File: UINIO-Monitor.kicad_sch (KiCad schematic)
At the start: 0 parts

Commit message: Start schematic drawing.
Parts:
- added C? (x5): 1uF, Capacitor_SMD:C_0402_1005Metric, symbol Device:C
- added CON? (x2): FFC_8Pin_0.5mm, Uinio:FPC-SMD_8P-P0.5_C9900011879, symbol Uinio:FFC_8Pin_0.5mm
- added D? (x5): 1N5819, Diode_THT:D_DO-41_SOD81_P10.16mm_Horizontal, symbol Diode:1N5819
- added J? (x2): Conn_01x08_Male, symbol Connector:Conn_01x08_Male
- added P?: LCD_Pad_12Pin, Uinio:ST7789-FPC-PAD, symbol Uinio:LCD_Pad_12Pin
- added P?: LCD_Pad_10Pin, symbol Uinio:LCD_Pad_10Pin
- added R?: 10K, symbol Device:R
- added R?: 10R, symbol Device:R
- added R? (x5): 4.7K, symbol Device:R
- added R?: 5.1R, symbol Device:R
- added R?: 20R, symbol Device:R
- added R?: 1K, symbol Device:R
- added U? (x2): ME6211C33M5G-N, Uinio:SOT-23-5_L3.0-W1.7-P0.95-LS2.8-BR, symbol Uinio:ME6211
- added VT?: S8050, Uinio:SOT-23-3_L2.9-W1.6-P1.90-LS2.9-BL, symbol Uinio:S8050
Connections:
- new net: P?.2 (LEDK), R?.2
- new net: C?.2, P?.3 (LEDA), P?.4 (VDD)
- new net: R?.1, R?.2, VT?.1 (B)
- new net: R?.1, VT?.3 (C)
- new net: CON?.1, J?.1 (Pin_1), R?.1
- new net: CON?.2, J?.2 (Pin_2), R?.1
- new net: CON?.3, J?.3 (Pin_3), R?.1
- new net: CON?.4, J?.4 (Pin_4), R?.1
- new net: CON?.5, J?.5 (Pin_5), R?.1
- new net: D?.2 (A), R?.2 (x5)
- new net: P?.1 (GND), R?.2
- new net: P?.9 (LEDA), R?.2
- new net 3.3V_1.3inch: C?.2, CON?.6, J?.6 (Pin_6), R?.1, U?.5 (Vout)
- new net 3.3V_2.4inch: C?.2, CON?.6, D?.1 (K), D?.1 (K), D?.1 (K), D?.1 (K), D?.1 (K), J?.6 (Pin_6), P?.2 (RESET), P?.3 (SCL), P?.4 (D/C), P?.5 (CS), P?.6 (SDA), P?.8 (VCC), U?.5 (Vout)
- new net 5V_1.3inch: C?.2, CON?.8, J?.8 (Pin_8), U?.1 (Vin), U?.3 (CE)
- new net 5V_2.4inch: C?.2, CON?.8, J?.8 (Pin_8), R?.1, U?.1 (Vin), U?.3 (CE)
- new net BLK: R?.2
- new net CS_1.3inch: CON?.1, J?.1 (Pin_1), P?.8 (CS)
- new net D/C_1.3inch: CON?.2, J?.2 (Pin_2), P?.7 (D/C)
- new net GND: C?.1, C?.1, C?.1, C?.1, C?.1, CON?.7, CON?.7, J?.7 (Pin_7), J?.7 (Pin_7), P?.1 (GND), P?.10 (LEDK), P?.12 (GND), P?.5 (GND), P?.6 (GND), R?.1, U?.2 (Vss), U?.2 (Vss), VT?.2 (E)
- new net RESET_1.3inch: CON?.3, J?.3 (Pin_3), P?.11 (RESET)
- new net SCL_1.3inch: CON?.5, J?.5 (Pin_5), P?.9 (SCL)
- new net SDA_1.3inch: CON?.4, J?.4 (Pin_4), P?.10 (SDA)
- no-connect marks 0 -> 3
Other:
- note added: "2.4 英寸"

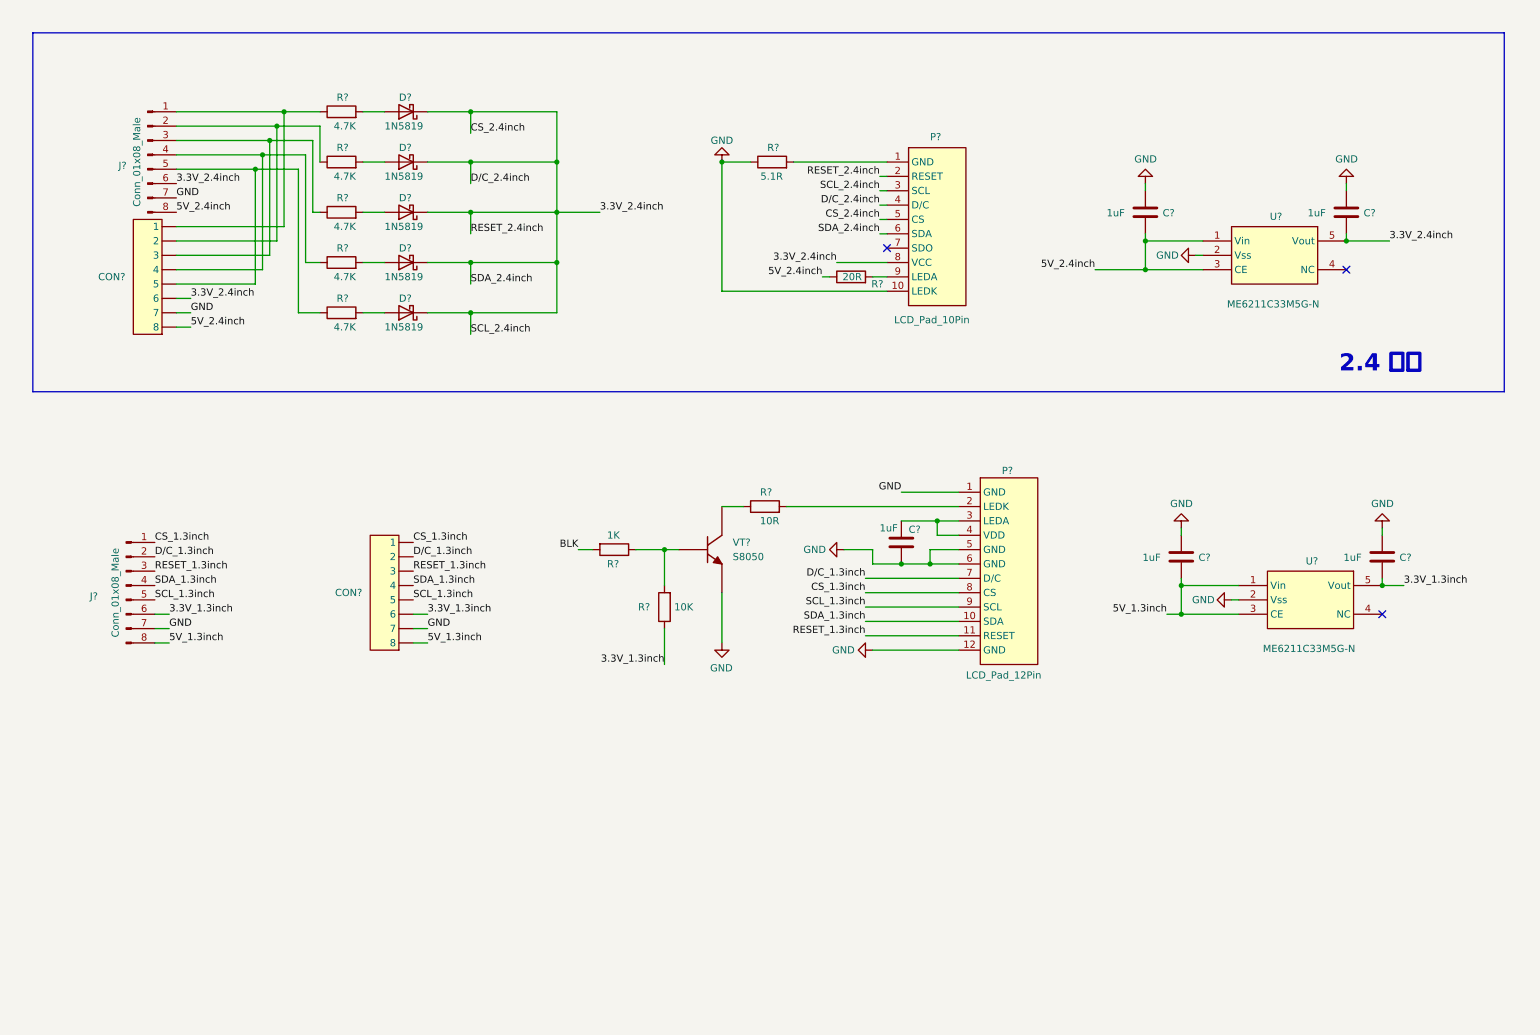
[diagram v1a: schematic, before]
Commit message: Redraw the schematic.
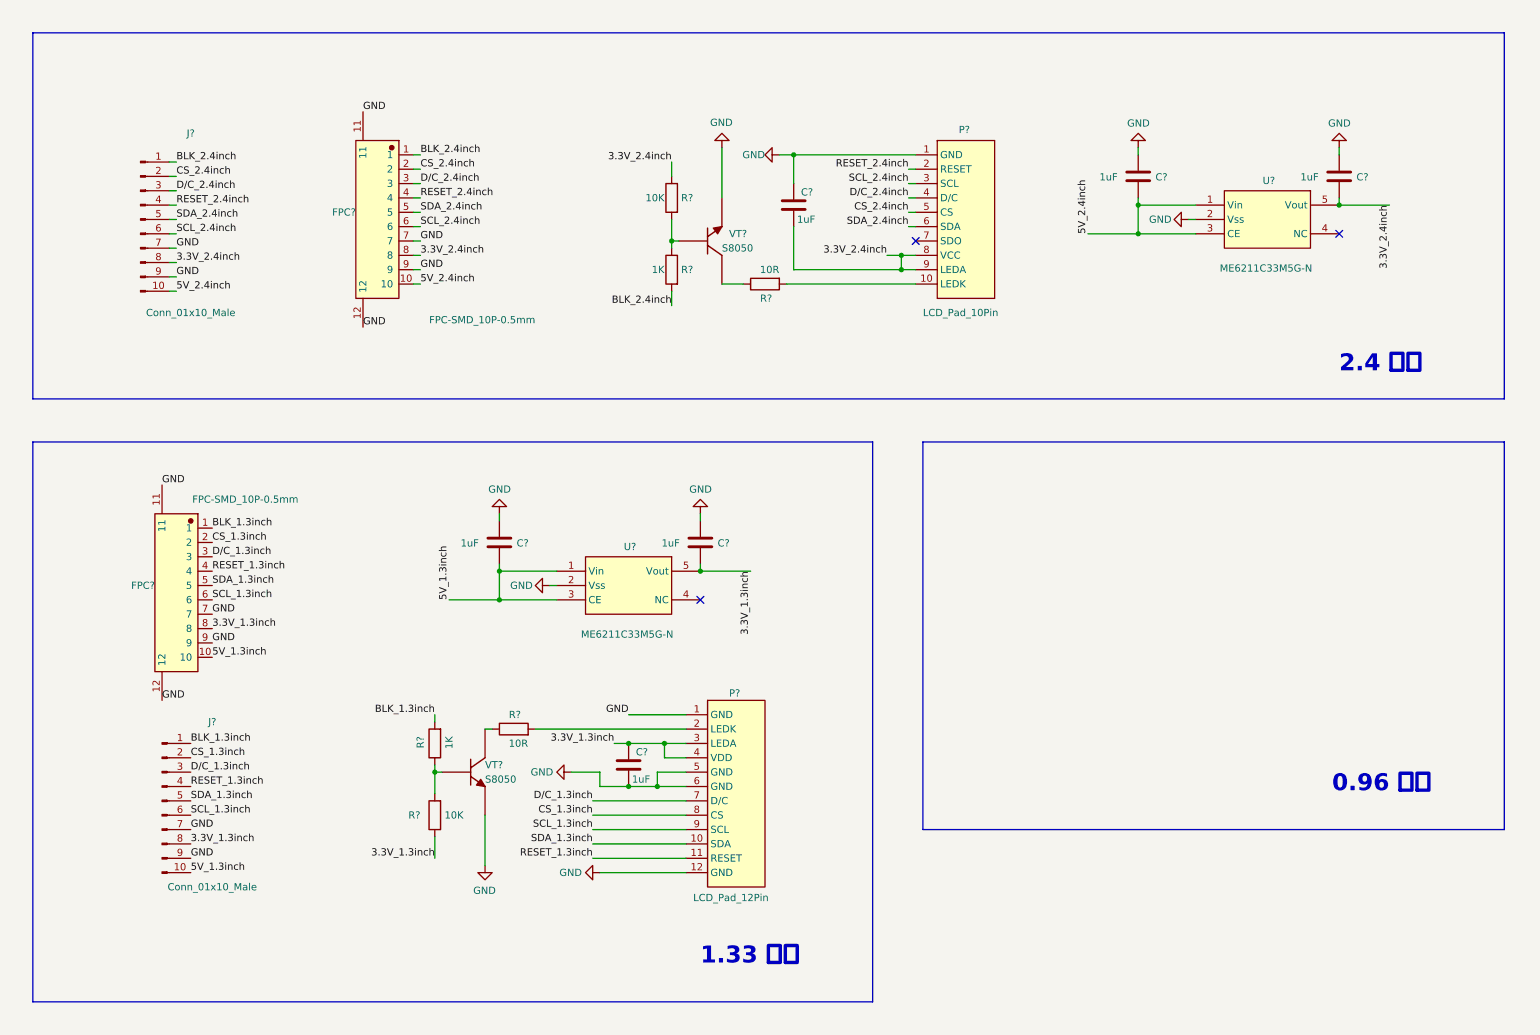
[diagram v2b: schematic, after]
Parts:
- removed C? (x2): 1uF, Capacitor_SMD:C_0402_1005Metric, symbol Device:C
- removed CON? (x2): FFC_8Pin_0.5mm, Uinio:FPC-SMD_8P-P0.5_C9900011879, symbol Uinio:FFC_8Pin_0.5mm
- removed D? (x5): 1N5819, Diode_THT:D_DO-41_SOD81_P10.16mm_Horizontal, symbol Diode:1N5819
- removed J? (x2): Conn_01x08_Male, symbol Connector:Conn_01x08_Male
- removed R? (x5): 4.7K, symbol Device:R
- removed R?: 5.1R, symbol Device:R
- removed R?: 20R, symbol Device:R
- removed U?: ME6211C33M5G-N, Uinio:SOT-23-5_L3.0-W1.7-P0.95-LS2.8-BR, symbol Uinio:ME6211
- added C? (x3): 1uF, Capacitor_SMD:C_0402_1005Metric, symbol Device:C
- added FPC? (x2): FPC-SMD_10P-0.5mm, Uinio:FPC-SMD_KH-FG0.5-H2.0-10Pin, symbol Uinio:FPC-SMD_10P-0.5mm
- added J? (x2): Conn_01x10_Male, symbol Connector:Conn_01x10_Male
- added R?: 10R, symbol Device:R
- added R?: 10K, symbol Device:R
- added R?: 1K, symbol Device:R
- added U?: ME6211C33M5G-N, Uinio:SOT-23-5_L3.0-W1.7-P0.95-LS2.8-BR, symbol Uinio:ME6211
- added VT?: S8050, Uinio:SOT-23-3_L2.9-W1.6-P1.90-LS2.9-BL, symbol Uinio:S8050
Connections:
- net 3.3V_1.3inch: now also C?.2, P?.3 (LEDA), P?.4 (VDD), FPC?.8, J?.8 (Pin_8)
- net 3.3V_2.4inch: now also P?.9 (LEDA), C?.1, C?.2, FPC?.8, J?.8 (Pin_8), R?.1, U?.5 (Vout); no longer P?.2 (RESET), P?.3 (SCL), P?.4 (D/C), P?.5 (CS), P?.6 (SDA)
- net 5V_1.3inch: now also FPC?.10, J?.10 (Pin_10)
- net 5V_2.4inch: now also C?.2, FPC?.10, J?.10 (Pin_10), U?.1 (Vin), U?.3 (CE)
- net CS_1.3inch: now also FPC?.2, J?.2 (Pin_2)
- net D/C_1.3inch: now also FPC?.3, J?.3 (Pin_3)
- net GND: now also P?.1 (GND), C?.1, C?.1, C?.2, FPC?.11, FPC?.11, FPC?.12, FPC?.12, FPC?.7, FPC?.7, FPC?.9, FPC?.9, J?.7 (Pin_7), J?.7 (Pin_7), J?.9 (Pin_9), J?.9 (Pin_9), U?.2 (Vss), VT?.2 (E); no longer P?.10 (LEDK)
- net RESET_1.3inch: now also FPC?.4, J?.4 (Pin_4)
- net SCL_1.3inch: now also FPC?.6, J?.6 (Pin_6)
- net SDA_1.3inch: now also FPC?.5, J?.5 (Pin_5)
- net BLK renamed BLK_1.3inch
- net BLK_1.3inch: now also FPC?.1, J?.1 (Pin_1)
- new net: R?.1, VT?.3 (C)
- new net: P?.10 (LEDK), R?.2
- new net: R?.1, R?.2, VT?.1 (B)
- new net BLK_2.4inch: FPC?.1, J?.1 (Pin_1), R?.2
- new net CS_2.4inch: FPC?.2, J?.2 (Pin_2), P?.5 (CS)
- new net D/C_2.4inch: FPC?.3, J?.3 (Pin_3), P?.4 (D/C)
- new net RESET_2.4inch: FPC?.4, J?.4 (Pin_4), P?.2 (RESET)
- new net SCL_2.4inch: FPC?.6, J?.6 (Pin_6), P?.3 (SCL)
- new net SDA_2.4inch: FPC?.5, J?.5 (Pin_5), P?.6 (SDA)
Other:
- note added: "0.96 英寸"
- note added: "1.33 英寸"
- moved on the sheet: C?, P?, R?, U?, VT?

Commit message: Redraw the schematic.
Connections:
- net 3.3V_1.3inch: now also FPC?.1, J?.1 (Pin_1); no longer FPC?.8, J?.8 (Pin_8)
- net 3.3V_2.4inch: now also FPC?.1, J?.1 (Pin_1); no longer FPC?.8, J?.8 (Pin_8)
- net BLK_1.3inch: now also FPC?.3, J?.3 (Pin_3); no longer FPC?.1, J?.1 (Pin_1)
- net BLK_2.4inch: now also FPC?.3, J?.3 (Pin_3); no longer FPC?.1, J?.1 (Pin_1)
- net CS_1.3inch: now also FPC?.4, J?.4 (Pin_4); no longer FPC?.2, J?.2 (Pin_2)
- net CS_2.4inch: now also FPC?.4, J?.4 (Pin_4); no longer FPC?.2, J?.2 (Pin_2)
- net D/C_1.3inch: now also FPC?.5, J?.5 (Pin_5); no longer FPC?.3, J?.3 (Pin_3)
- net D/C_2.4inch: now also FPC?.5, J?.5 (Pin_5); no longer FPC?.3, J?.3 (Pin_3)
- net GND: now also FPC?.2, FPC?.2, J?.2 (Pin_2), J?.2 (Pin_2); no longer FPC?.7, FPC?.7, J?.7 (Pin_7), J?.7 (Pin_7)
- net RESET_1.3inch: now also FPC?.6, J?.6 (Pin_6); no longer FPC?.4, J?.4 (Pin_4)
- net RESET_2.4inch: now also FPC?.6, J?.6 (Pin_6); no longer FPC?.4, J?.4 (Pin_4)
- net SCL_1.3inch: now also FPC?.8, J?.8 (Pin_8); no longer FPC?.6, J?.6 (Pin_6)
- net SCL_2.4inch: now also FPC?.8, J?.8 (Pin_8); no longer FPC?.6, J?.6 (Pin_6)
- net SDA_1.3inch: now also FPC?.7, J?.7 (Pin_7); no longer FPC?.5, J?.5 (Pin_5)
- net SDA_2.4inch: now also FPC?.7, J?.7 (Pin_7); no longer FPC?.5, J?.5 (Pin_5)
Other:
- moved on the sheet: C?, FPC?, J?, P?, R?, U?, VT?

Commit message: Complete schematic drawing.
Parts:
- removed J? (x2): Conn_01x10_Male, symbol Connector:Conn_01x10_Male
- added C10, C11, C12, C13, C8, C9: C, Capacitor_SMD:C_0402_1005Metric, symbol Device:C
- added C7: C, Capacitor_SMD:C_0603_1608Metric, symbol Device:C
- added D1: 1N4148W, Diode_SMD:D_SOD-123, symbol Diode:1N4148W
- added J1, J2: Conn_01x09_Male, Connector_PinHeader_2.54mm:PinHeader_1x09_P2.54mm_Vertical, symbol Connector:Conn_01x09_Male
- added J3: Conn_01x04_Male, Connector_PinHeader_2.54mm:PinHeader_1x04_P2.54mm_Vertical, symbol Connector:Conn_01x04_Male
- added P3: OLED_Pad_30Pin, Uinio:OLED_Pad_30Pin, symbol Uinio:OLED_Pad_30Pin
- added R10, R7, R8, R9: R, Resistor_SMD:R_0402_1005Metric, symbol Device:R
- added U3: XC6206PxxxMR, Package_TO_SOT_SMD:SOT-23-3, symbol Regulator_Linear:XC6206PxxxMR
- C1, C2, C3, C4, C5, C6: renamed from C?; value 1uF -> C; footprint Capacitor_SMD:C_0402_1005Metric -> Capacitor_SMD:C_0603_1608Metric
- P1: renamed from P?; footprint (none) -> Uinio:LCD_Pad_10Pin
- P2: renamed from P?; footprint Uinio:ST7789-FPC-PAD -> Uinio:LCD_Pad_12Pin
- R1, R4: renamed from R?; value 10K -> R; footprint (none) -> Resistor_SMD:R_0603_1608Metric
- R2, R3: renamed from R?; value 1K -> R; footprint (none) -> Resistor_SMD:R_0603_1608Metric
- R5, R6: renamed from R?; value 10R -> R; footprint (none) -> Resistor_SMD:R_0603_1608Metric
- U1, U2: renamed from U?; value ME6211C33M5G-N -> ME6211
- gave numbers to parts that had none: 4
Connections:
- net 3.3V_1.3inch: now also J1.7 (Pin_7)
- net 3.3V_2.4inch: now also J2.7 (Pin_7)
- net 5V_1.3inch: now also J1.9 (Pin_9)
- net 5V_2.4inch: now also J2.9 (Pin_9)
- net BLK_1.3inch: now also J1.1 (Pin_1)
- net BLK_2.4inch: now also J2.1 (Pin_1)
- net CS_1.3inch: now also J1.2 (Pin_2)
- net CS_2.4inch: now also J2.2 (Pin_2)
- net D/C_1.3inch: now also J1.3 (Pin_3)
- net D/C_2.4inch: now also J2.3 (Pin_3)
- net GND: now also C10.2, C11.2, C7.1, C8.1, C9.1, J1.8 (Pin_8), J2.8 (Pin_8), J3.3 (Pin_3), P3.1 (NC), P3.10 (BS0), P3.12 (BS2), P3.13 (CS), P3.15 (D/C), P3.16 (RW), P3.17 (RD), P3.21 (D3), P3.22 (D4), P3.23 (D5), P3.24 (D6), P3.25 (D7), P3.29 (VLSS), P3.30 (NC), P3.8 (VSS), R10.1, U3.1 (GND)
- net RESET_1.3inch: now also J1.4 (Pin_4)
- net RESET_2.4inch: now also J2.4 (Pin_4)
- net SCL_1.3inch: now also J1.6 (Pin_6)
- net SCL_2.4inch: now also J2.6 (Pin_6)
- net SDA_1.3inch: now also J1.5 (Pin_5)
- net SDA_2.4inch: now also J2.5 (Pin_5)
- new net: C8.2, C9.2, D1.1 (K), P3.11 (BS1), P3.6 (VBAT), P3.9 (VDD), R7.2, R8.2, R9.2, U3.2 (VO)
- new net: C13.1, P3.5 (C1N)
- new net: C13.2, P3.4 (C1P)
- new net: C12.1, P3.3 (C2N)
- new net: C12.2, P3.2 (C2P)
- new net: P3.26 (IREF), R10.2
- new net: C10.1, P3.27 (VCOMH)
- new net: C11.1, P3.28 (VCC)
- new net RESET_0.96inch: C7.2, D1.2 (A), P3.14 (RESET), R9.1
- new net SCK_0.96inch: J3.1 (Pin_1), P3.18 (D0), R7.1
- new net SDA_0.96inch: J3.2 (Pin_2), P3.19 (D1), P3.20 (D2), R8.1
- new net VCC_0.96inch: J3.4 (Pin_4), U3.3 (VI)
- no-connect marks 3 -> 4
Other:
- note added: "0.96 英寸 SSD1315 OLED 屏幕基板"
- note added: "1.33 英寸 ST7789 LCD 屏幕基板"
- note added: "2.4 英寸 ST7789 LCD 屏幕基板"
- note removed: "0.96 英寸"
- note removed: "1.33 英寸"
- note removed: "2.4 英寸"
- moved on the sheet: C1, C2, C3, C4, C5, C6, FPC1, FPC2, P1, P2, R1, R2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

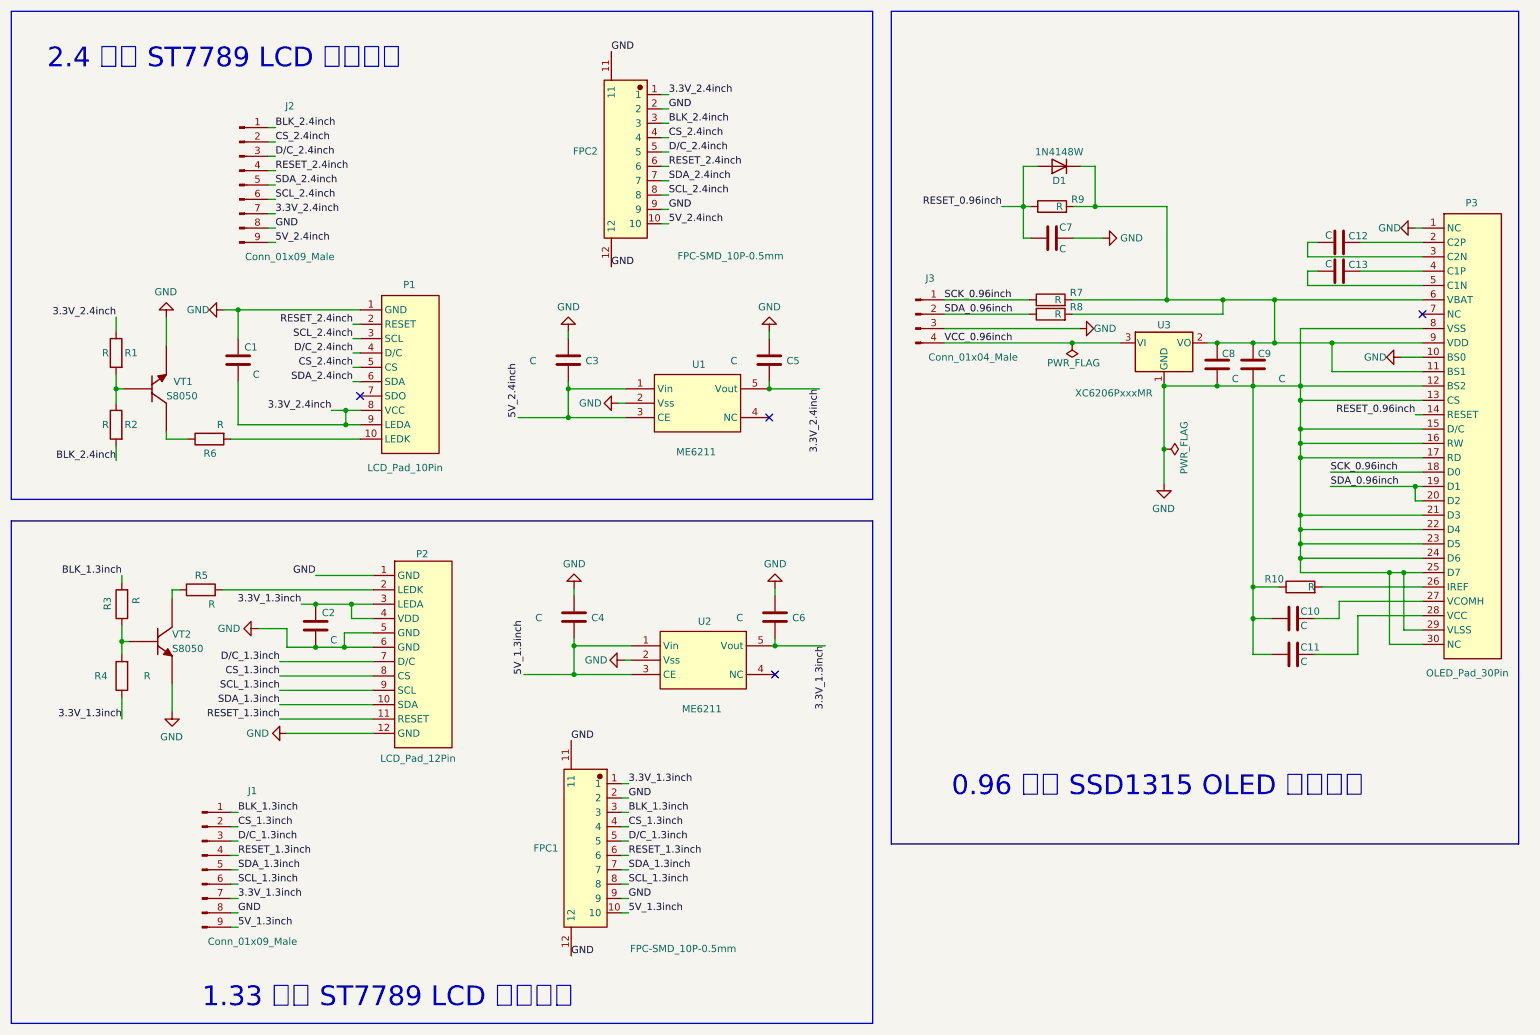
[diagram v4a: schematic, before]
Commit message: Complete component layout.
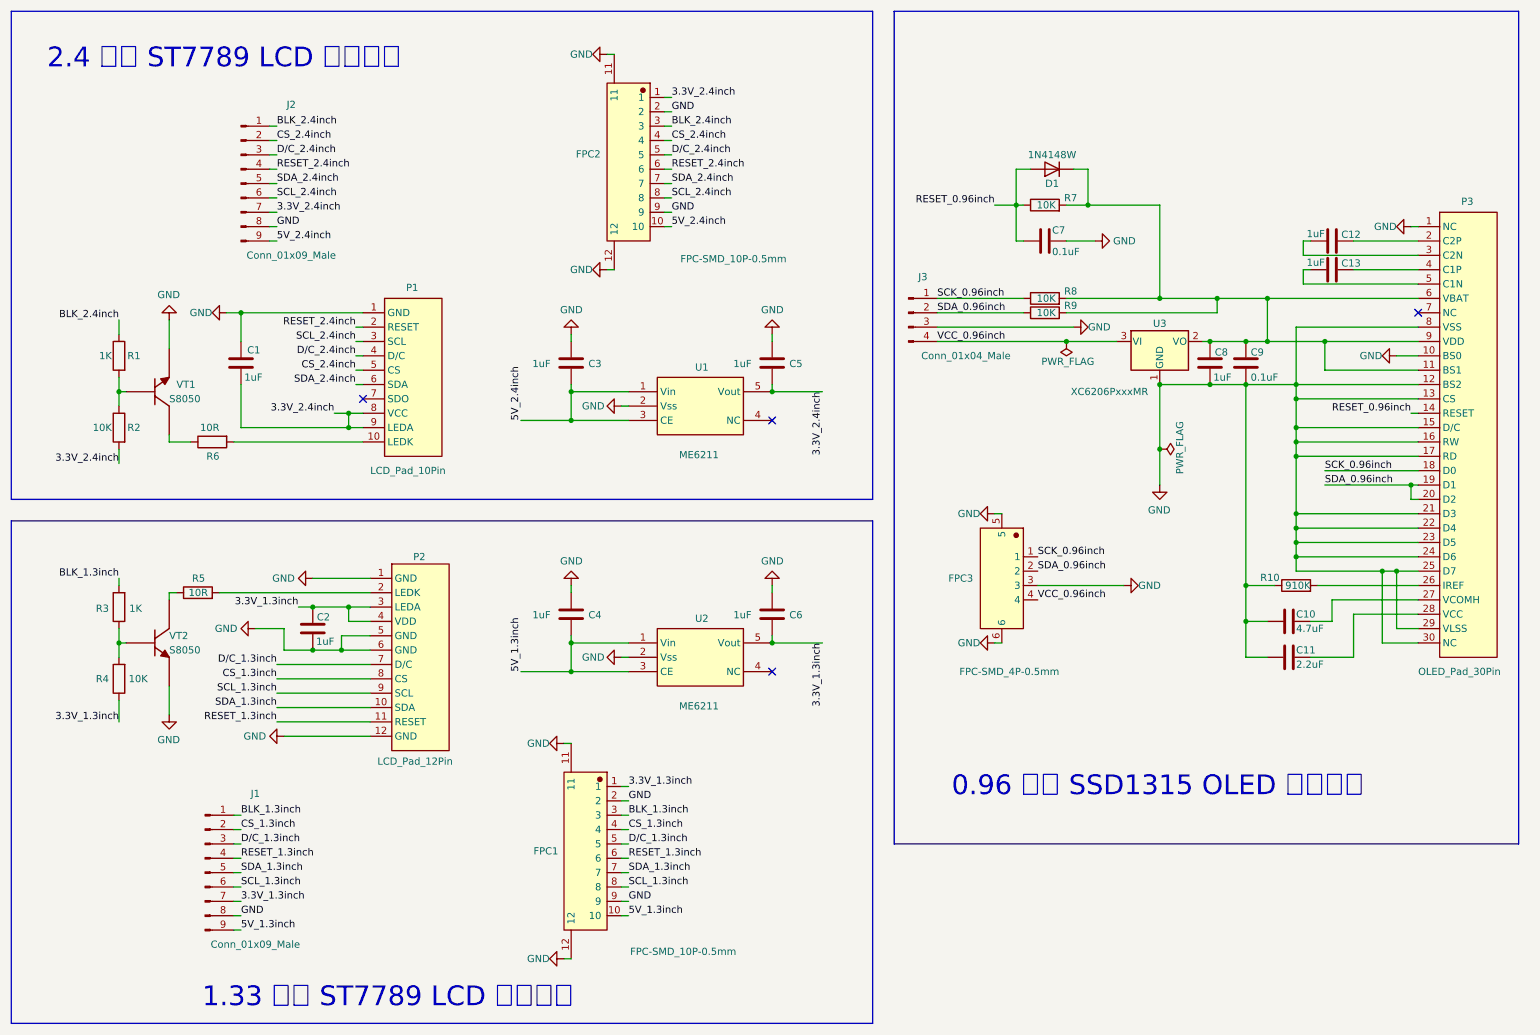
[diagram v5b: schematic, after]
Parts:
- added FPC3: FPC-SMD_4P-0.5mm, Uinio:FPC-SMD_4P-P0.5, symbol Uinio:FPC-SMD_4P-0.5mm
- C1, C12, C13, C2, C3, C4, C5, C6, C8: value C -> 1uF
- C10: value C -> 4.7uF
- C11: value C -> 2.2uF
- C7: value C -> 0.1uF; footprint Capacitor_SMD:C_0603_1608Metric -> Capacitor_SMD:C_0402_1005Metric
- C9: value C -> 0.1uF
- R1, R3: value R -> 1K
- R10: value R -> 910K
- R2, R4: value R -> 10K
- R5, R6: value R -> 10R
- R7: renamed from R9; value R -> 10K
- R8: renamed from R7; value R -> 10K
- R9: renamed from R8; value R -> 10K
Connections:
- net 3.3V_2.4inch: now also R2.2; no longer R1.1
- net BLK_2.4inch: now also R1.1; no longer R2.2
- net GND: now also FPC3.3, FPC3.5, FPC3.6
- net SCK_0.96inch: now also FPC3.1
- net SDA_0.96inch: now also FPC3.2
- net VCC_0.96inch: now also FPC3.4
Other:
- moved on the sheet: C1, C10, C11, C12, C13, C2, C3, C4, C5, C6, C7, C8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
